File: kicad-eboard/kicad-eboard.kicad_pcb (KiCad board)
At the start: 2 copper layers, 92 parts, among them J1 Conn_01x02, J19 Conn_01x10, SW10 AMT10_Encoder, SW4 LIMIT_1, SW5 LIMIT_2, SW6 AMT10_Encoder, SW7 AMT10_Encoder, SW8 AMT10_Encoder, SW9 AMT10_Encoder, U1 TinkerBoard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

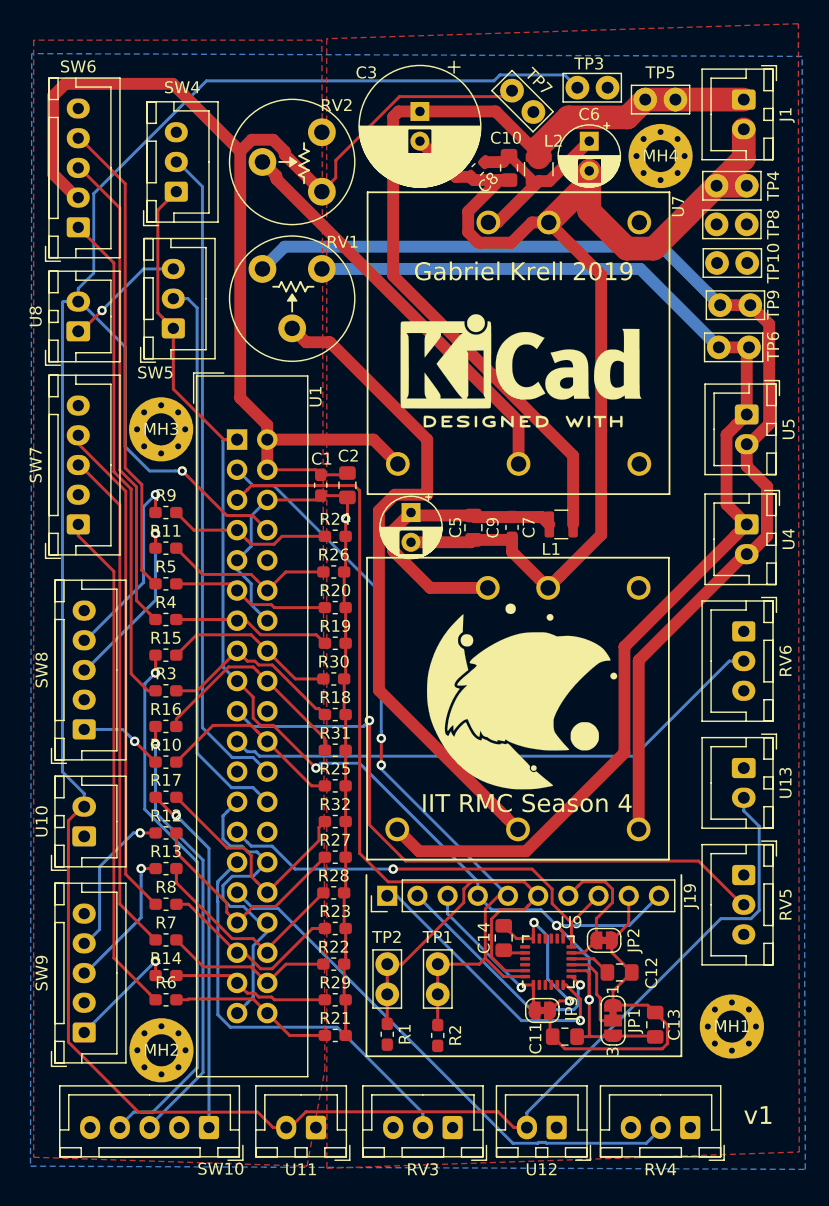
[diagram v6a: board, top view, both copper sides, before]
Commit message: Add readable test point silkscreens
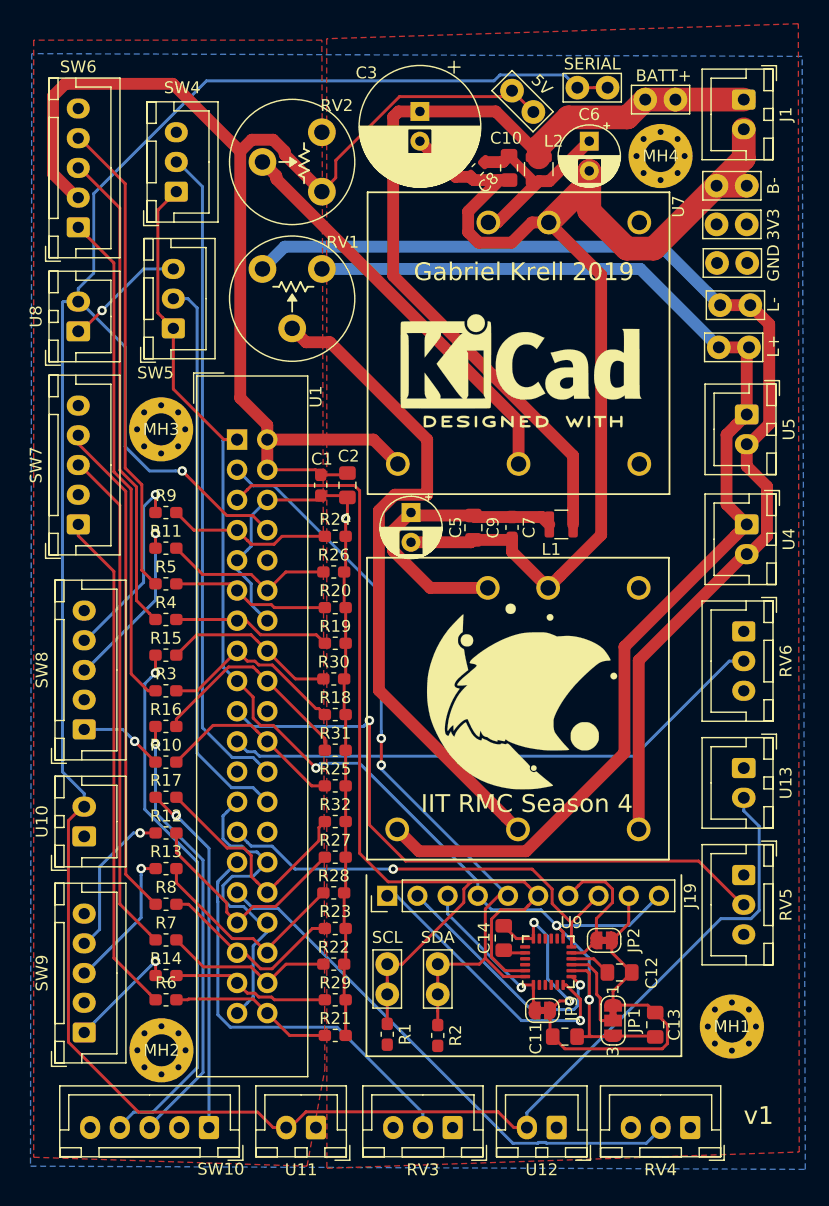
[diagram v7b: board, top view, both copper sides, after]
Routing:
- net Net-(TP3-Pad1): track 229.2 -> 231.7 mm
- net +5V: track 104.5 -> 107.0 mm
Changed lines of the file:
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@@
     (thickness 1.6)
     (drawings 6)
-    (tracks 673)
+    (tracks 676)
     (zones 0)
     (modules 92)
@@
     (descr "wire loop as test point, pitch 2.54mm, hole diameter 1.0mm, wire diameter 0.8mm")
     (tags "test point wire loop")
-    (fp_text reference TP8 (at -2.25 0 90) (layer F.SilkS)
+    (fp_text reference TP8 (at -2.25 0 90) (layer F.SilkS) hide
       (effects (font (size 1 1) (thickness 0.15)))
     )
@@
       (effects (font (size 1 1) (thickness 0.15)))
     )
-    (fp_text user %R (at 1.1 2.1) (layer F.Fab)
+    (fp_text user 3V3 (at -2.25 0 270) (layer F.SilkS)
       (effects (font (size 1 1) (thickness 0.15)))
     )
-    (fp_line (start -1.2 -1.2) (end -1.2 1.2) (layer F.SilkS) (width 0.12))
-    (fp_line (start -1.2 1.2) (end 3.7 1.2) (layer F.SilkS) (width 0.12))
-    (fp_line (start 3.7 1.2) (end 3.7 -1.2) (layer F.SilkS) (width 0.12))
-    (fp_line (start 3.7 -1.2) (end -1.2 -1.2) (layer F.SilkS) (width 0.12))
-    (fp_line (start 2.54 0) (end 0 0) (layer F.Fab) (width 0.12))
-    (fp_line (start -1.5 -1.5) (end 4.04 -1.5) (layer F.CrtYd) (width 0.05))
-    (fp_line (start -1.5 -1.5) (end -1.5 1.5) (layer F.CrtYd) (width 0.05))
-    (fp_line (start 4.04 1.5) (end 4.04 -1.5) (layer F.CrtYd) (width 0.05))
     (fp_line (start 4.04 1.5) (end -1.5 1.5) (layer F.CrtYd) (width 0.05))
-    (pad 1 thru_hole circle (at 0 0 180) (size 2 2) (drill 1) (layers *.Cu *.Mask)
-      (net 9 +3V3))
+    (fp_line (start 4.04 1.5) (end 4.04 -1.5) (layer F.CrtYd) (width 0.05))
+    (fp_line (start -1.5 -1.5) (end -1.5 1.5) (layer F.CrtYd) (width 0.05))
+    (fp_line (start -1.5 -1.5) (end 4.04 -1.5) (layer F.CrtYd) (width 0.05))
+    (fp_line (start 2.54 0) (end 0 0) (layer F.Fab) (width 0.12))
+    (fp_line (start 3.7 -1.2) (end -1.2 -1.2) (layer F.SilkS) (width 0.12))
+    (fp_line (start 3.7 1.2) (end 3.7 -1.2) (layer F.SilkS) (width 0.12))
+    (fp_line (start -1.2 1.2) (end 3.7 1.2) (layer F.SilkS) (width 0.12))
+    (fp_line (start -1.2 -1.2) (end -1.2 1.2) (layer F.SilkS) (width 0.12))
+    (fp_text user %R (at 1.1 2.1) (layer F.Fab)
+      (effects (font (size 1 1) (thickness 0.15)))
+    )
     (pad 1 thru_hole circle (at 2.54 0 180) (size 2 2) (drill 1) (layers *.Cu *.Mask)
       (net 9 +3V3))
+    (pad 1 thru_hole circle (at 0 0 180) (size 2 2) (drill 1) (layers *.Cu *.Mask)
+      (net 9 +3V3))
     (model ${KISYS3DMOD}/TestPoint.3dshapes/TestPoint_Bridge_Pitch2.54mm_Drill1.0mm.wrl
       (at (xyz 0 0 0))
@@
     (descr "wire loop as test point, pitch 2.54mm, hole diameter 1.0mm, wire diameter 0.8mm")
     (tags "test point wire loop")
-    (fp_text reference TP7 (at 1.06066 -2.12132 315) (layer F.SilkS)
+    (fp_text reference TP7 (at 1.06066 -2.12132 315) (layer F.SilkS) hide
       (effects (font (size 1 1) (thickness 0.15)))
     )
@@
       (effects (font (size 1 1) (thickness 0.15)))
     )
+    (fp_text user 5V (at 1.414214 -2.12132 315) (layer F.SilkS)
+      (effects (font (size 1 1) (thickness 0.15)))
+    )
     (pad 1 thru_hole circle (at 2.54 0 315) (size 2 2) (drill 1) (layers *.Cu *.Mask)
       (net 10 +5V))
@@
     (descr "wire loop as test point, pitch 2.54mm, hole diameter 1.0mm, wire diameter 0.8mm")
     (tags "test point wire loop")
-    (fp_text reference TP10 (at -2.21 0 90) (layer F.SilkS)
+    (fp_text reference TP10 (at -2.21 0 90) (layer F.SilkS) hide
       (effects (font (size 1 1) (thickness 0.15)))
     )
@@
       (effects (font (size 1 1) (thickness 0.15)))
     )
+    (fp_text user GND (at -2.21 0 270) (layer F.SilkS)
+      (effects (font (size 1 1) (thickness 0.15)))
+    )
     (pad 1 thru_hole circle (at 2.54 0 180) (size 2 2) (drill 1) (layers *.Cu *.Mask)
       (net 7 GND))
@@
     (descr "wire loop as test point, pitch 2.54mm, hole diameter 1.0mm, wire diameter 0.8mm")
     (tags "test point wire loop")
-    (fp_text reference TP3 (at 1 -2 180) (layer F.SilkS)
+    (fp_text reference TP3 (at 1 -2 180) (layer F.SilkS) hide
       (effects (font (size 1 1) (thickness 0.15)))
     )
@@
     (fp_line (start 4.04 1.5) (end 4.04 -1.5) (layer F.CrtYd) (width 0.05))
     (fp_line (start 4.04 1.5) (end -1.5 1.5) (layer F.CrtYd) (width 0.05))
+    (fp_text user SERIAL (at 1.25 -2) (layer F.SilkS)
+      (effects (font (size 1 1) (thickness 0.15)))
+    )
     (pad 1 thru_hole circle (at 0 0) (size 2 2) (drill 1) (layers *.Cu *.Mask)
       (net 3 "Net-(TP3-Pad1)"))
@@
     (descr "wire loop as test point, pitch 2.54mm, hole diameter 1.0mm, wire diameter 0.8mm")
     (tags "test point wire loop")
-    (fp_text reference TP9 (at -1.95 0.05 270) (layer F.SilkS)
+    (fp_text reference TP9 (at -1.95 0.05 270) (layer F.SilkS) hide
       (effects (font (size 1 1) (thickness 0.15)))
     )
@@
     (fp_line (start 4.04 1.5) (end 4.04 -1.5) (layer F.CrtYd) (width 0.05))
     (fp_line (start 4.04 1.5) (end -1.5 1.5) (layer F.CrtYd) (width 0.05))
+    (fp_text user L- (at -1.95 0.05 270) (layer F.SilkS)
+      (effects (font (size 1 1) (thickness 0.15)))
+    )
     (pad 1 thru_hole circle (at 0 0 180) (size 2 2) (drill 1) (layers *.Cu *.Mask)
       (net 8 GNDA))
@@
     (descr "wire loop as test point, pitch 2.54mm, hole diameter 1.0mm, wire diameter 0.8mm")
     (tags "test point wire loop")
-    (fp_text reference TP5 (at 1.25 2.25) (layer F.SilkS)
+    (fp_text reference TP5 (at 1.25 2.25) (layer F.SilkS) hide
       (effects (font (size 1 1) (thickness 0.15)))
     )
@@
     (fp_line (start 4.04 1.5) (end 4.04 -1.5) (layer F.CrtYd) (width 0.05))
     (fp_line (start 4.04 1.5) (end -1.5 1.5) (layer F.CrtYd) (width 0.05))
+    (fp_text user BATT+ (at 1 2 180) (layer F.SilkS)
+      (effects (font (size 1 1) (thickness 0.15)))
+    )
     (pad 1 thru_hole circle (at 0 0 180) (size 2 2) (drill 1) (layers *.Cu *.Mask)
       (net 6 +BATT))
@@
     (descr "wire loop as test point, pitch 2.54mm, hole diameter 1.0mm, wire diameter 0.8mm")
     (tags "test point wire loop")
-    (fp_text reference TP1 (at -2.25 0 180) (layer F.SilkS)
+    (fp_text reference TP1 (at -2.25 0 180) (layer F.SilkS) hide
       (effects (font (size 1 1) (thickness 0.15)))
     )
@@
       (effects (font (size 1 1) (thickness 0.15)))
     )
+    (fp_text user SDA (at -2.25 0) (layer F.SilkS)
+      (effects (font (size 1 1) (thickness 0.15)))
+    )
     (pad 1 thru_hole circle (at 2.54 0 270) (size 2 2) (drill 1) (layers *.Cu *.Mask)
       (net 5 /IMU/SDA))
@@
     (descr "wire loop as test point, pitch 2.54mm, hole diameter 1.0mm, wire diameter 0.8mm")
     (tags "test point wire loop")
-    (fp_text reference TP2 (at -2.25 0 180) (layer F.SilkS)
+    (fp_text reference TP2 (at -2.25 0 180) (layer F.SilkS) hide
       (effects (font (size 1 1) (thickness 0.15)))
     )
@@
     (fp_line (start 4.04 1.5) (end 4.04 -1.5) (layer F.CrtYd) (width 0.05))
     (fp_line (start 4.04 1.5) (end -1.5 1.5) (layer F.CrtYd) (width 0.05))
+    (fp_text user SCL (at -2.25 0) (layer F.SilkS)
+      (effects (font (size 1 1) (thickness 0.15)))
+    )
     (pad 1 thru_hole circle (at 0 0 270) (size 2 2) (drill 1) (layers *.Cu *.Mask)
       (net 4 /IMU/SCL))
@@
     (descr "wire loop as test point, pitch 2.54mm, hole diameter 1.0mm, wire diameter 0.8mm")
     (tags "test point wire loop")
-    (fp_text reference TP4 (at -2.25 0 90) (layer F.SilkS)
+    (fp_text reference TP4 (at -2.25 0 90) (layer F.SilkS) hide
       (effects (font (size 1 1) (thickness 0.15)))
     )
@@
     (fp_line (start 4.04 1.5) (end 4.04 -1.5) (layer F.CrtYd) (width 0.05))
     (fp_line (start 4.04 1.5) (end -1.5 1.5) (layer F.CrtYd) (width 0.05))
+    (fp_text user B- (at -2.25 0 270) (layer F.SilkS)
+      (effects (font (size 1 1) (thickness 0.15)))
+    )
     (pad 1 thru_hole circle (at 0 0 180) (size 2 2) (drill 1) (layers *.Cu *.Mask)
       (net 2 GNDPWR))
@@
     (descr "wire loop as test point, pitch 2.54mm, hole diameter 1.0mm, wire diameter 0.8mm")
     (tags "test point wire loop")
-    (fp_text reference TP6 (at 4.6 -0.1 270) (layer F.SilkS)
+    (fp_text reference TP6 (at 4.6 -0.1 270) (layer F.SilkS) hide
       (effects (font (size 1 1) (thickness 0.15)))
     )
@@
       (effects (font (size 1 1) (thickness 0.15)))
     )
+    (fp_text user L+ (at 4.6 -0.1 90) (layer F.SilkS)
+      (effects (font (size 1 1) (thickness 0.15)))
+    )
     (pad 1 thru_hole circle (at 2.54 0) (size 2 2) (drill 1) (layers *.Cu *.Mask)
       (net 1 +12V))
@@
   (segment (start 52.485999 15.174999) (end 52.985999 14.674999) (width 0.25) (layer B.Cu) (net 3))
   (segment (start 28.288286 15.174999) (end 52.485999 15.174999) (width 0.25) (layer B.Cu) (net 3))
+  (segment (start 60.914213 15.75) (end 62.04 15.75) (width 0.25) (layer F.Cu) (net 3))
+  (segment (start 59.5 15.75) (end 60.914213 15.75) (width 0.25) (layer F.Cu) (net 3))
   (segment (start 43.5 90.914213) (end 43.5 92.04) (width 0.25) (layer F.Cu) (net 4))
   (segment (start 43.5 89.5) (end 43.5 90.914213) (width 0.25) (layer F.Cu) (net 4))
@@
   (segment (start 16.408269 15.424991) (end 15.374979 16.458281) (width 1) (layer F.Cu) (net 10))
   (segment (start 25.452591 15.424991) (end 16.408269 15.424991) (width 1) (layer F.Cu) (net 10))
+  (segment (start 54 16) (end 55.796051 17.796051) (width 0.25) (layer F.Cu) (net 10))
   (segment (start 55.8 93.3) (end 55.9 93.4) (width 0.25) (layer F.Cu) (net 11))
   (segment (start 55.8 91.25) (end 55.8 93.3) (width 0.25) (layer F.Cu) (net 11))

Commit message: Clean up perimeter silkscreen
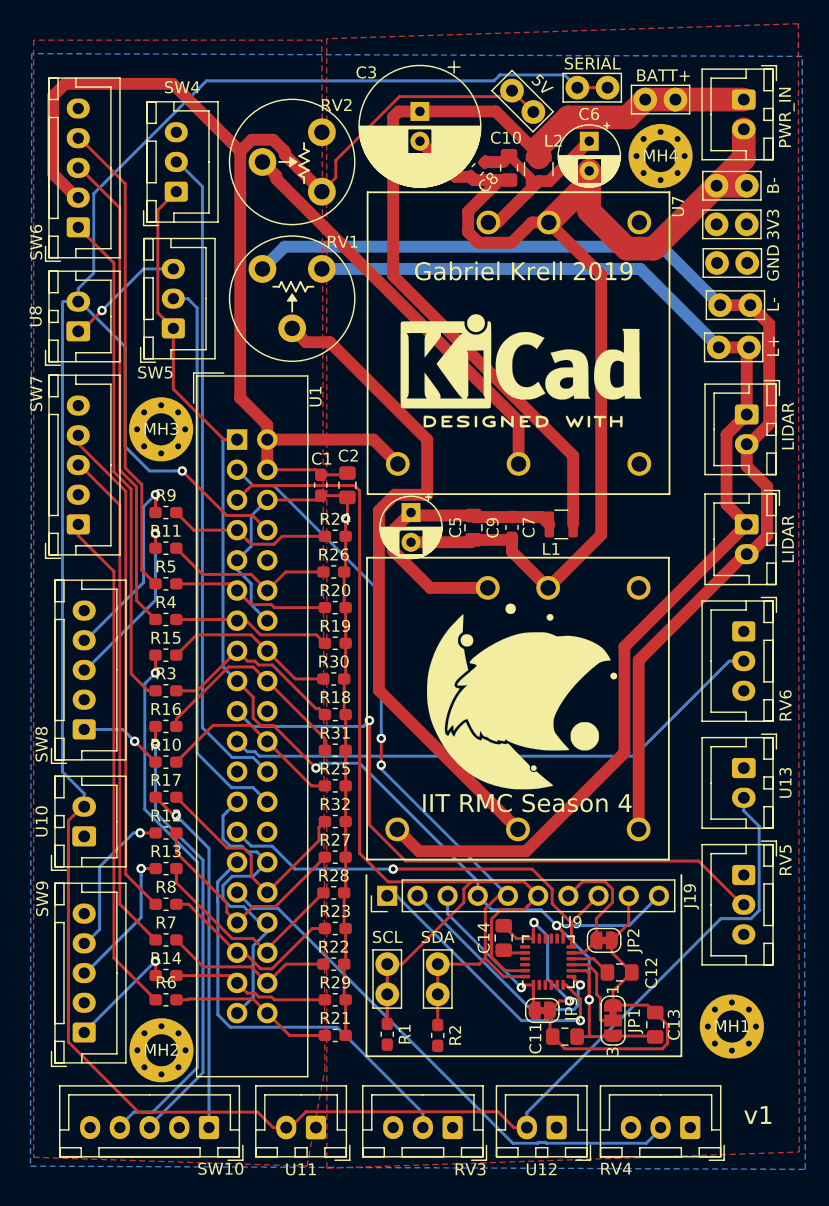
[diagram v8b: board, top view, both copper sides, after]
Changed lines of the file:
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@@
     (descr "JST XH series connector, B3B-XH-A (http://www.jst-mfg.com/product/pdf/eng/eXH.pdf), generated with kicad-footprint-generator")
     (tags "connector JST XH vertical")
-    (fp_text reference RV5 (at 2.5 -3.55 90) (layer F.SilkS)
+    (fp_text reference RV5 (at -1.25 -3.55 90) (layer F.SilkS)
       (effects (font (size 1 1) (thickness 0.15)))
     )
@@
     (descr "JST XH series connector, B3B-XH-A (http://www.jst-mfg.com/product/pdf/eng/eXH.pdf), generated with kicad-footprint-generator")
     (tags "connector JST XH vertical")
-    (fp_text reference RV6 (at 2.5 -3.55 90) (layer F.SilkS)
+    (fp_text reference RV6 (at 6.25 -3.55 90) (layer F.SilkS)
       (effects (font (size 1 1) (thickness 0.15)))
     )
@@
     (descr "JST XH series connector, B3B-XH-A (http://www.jst-mfg.com/product/pdf/eng/eXH.pdf), generated with kicad-footprint-generator")
     (tags "connector JST XH vertical")
-    (fp_text reference RV3 (at 2.5 -3.55) (layer F.SilkS)
+    (fp_text reference RV3 (at -1.5 -3.55) (layer F.SilkS)
       (effects (font (size 1 1) (thickness 0.15)))
     )
@@
     (descr "JST XH series connector, B2B-XH-A (http://www.jst-mfg.com/product/pdf/eng/eXH.pdf), generated with kicad-footprint-generator")
     (tags "connector JST XH vertical")
-    (fp_text reference J1 (at 1.25 -3.55 90) (layer F.SilkS)
+    (fp_text reference J1 (at 1.25 -3.55 90) (layer F.SilkS) hide
       (effects (font (size 1 1) (thickness 0.15)))
     )
@@
     (fp_line (start -2.85 -2.75) (end -2.85 -1.5) (layer F.SilkS) (width 0.12))
     (fp_text user %R (at 1.25 2.7 90) (layer F.Fab)
+      (effects (font (size 1 1) (thickness 0.15)))
+    )
+    (fp_text user PWR_IN (at 1.5 -3.5 270) (layer F.SilkS)
       (effects (font (size 1 1) (thickness 0.15)))
     )
@@
     (descr "JST XH series connector, B2B-XH-A (http://www.jst-mfg.com/product/pdf/eng/eXH.pdf), generated with kicad-footprint-generator")
     (tags "connector JST XH vertical")
-    (fp_text reference U4 (at 1.25 -3.55 90) (layer F.SilkS)
+    (fp_text reference U4 (at 1.25 -3.55 90) (layer F.SilkS) hide
       (effects (font (size 1 1) (thickness 0.15)))
     )
@@
     (fp_line (start -2.45 3.4) (end 4.95 3.4) (layer F.Fab) (width 0.1))
     (fp_line (start -2.45 -2.35) (end -2.45 3.4) (layer F.Fab) (width 0.1))
+    (fp_text user LIDAR (at 1.25 -3.5 270) (layer F.SilkS)
+      (effects (font (size 1 1) (thickness 0.15)))
+    )
     (pad 2 thru_hole oval (at 2.5 0 270) (size 1.7 2) (drill 1) (layers *.Cu *.Mask)
       (net 8 GNDA))
@@
     (descr "JST XH series connector, B2B-XH-A (http://www.jst-mfg.com/product/pdf/eng/eXH.pdf), generated with kicad-footprint-generator")
     (tags "connector JST XH vertical")
-    (fp_text reference U5 (at 1.25 -3.55 90) (layer F.SilkS)
+    (fp_text reference U5 (at 1.25 -3.55 90) (layer F.SilkS) hide
       (effects (font (size 1 1) (thickness 0.15)))
     )
@@
     (fp_line (start -2.45 3.4) (end 4.95 3.4) (layer F.Fab) (width 0.1))
     (fp_line (start -2.45 -2.35) (end -2.45 3.4) (layer F.Fab) (width 0.1))
+    (fp_text user LIDAR (at 1 -3.5 270) (layer F.SilkS)
+      (effects (font (size 1 1) (thickness 0.15)))
+    )
     (pad 2 thru_hole oval (at 2.5 0 270) (size 1.7 2) (drill 1) (layers *.Cu *.Mask)
       (net 8 GNDA))
@@
     (descr "JST XH series connector, B3B-XH-A (http://www.jst-mfg.com/product/pdf/eng/eXH.pdf), generated with kicad-footprint-generator")
     (tags "connector JST XH vertical")
-    (fp_text reference RV4 (at 2.5 -3.55) (layer F.SilkS)
+    (fp_text reference RV4 (at 6.25 -3.5) (layer F.SilkS)
       (effects (font (size 1 1) (thickness 0.15)))
     )
@@
     (descr "JST XH series connector, B5B-XH-A (http://www.jst-mfg.com/product/pdf/eng/eXH.pdf), generated with kicad-footprint-generator")
     (tags "connector JST XH vertical")
-    (fp_text reference SW6 (at 13.5 0) (layer F.SilkS)
+    (fp_text reference SW6 (at -1.25 -3.5 90) (layer F.SilkS)
       (effects (font (size 1 1) (thickness 0.15)))
     )
@@
     (descr "JST XH series connector, B5B-XH-A (http://www.jst-mfg.com/product/pdf/eng/eXH.pdf), generated with kicad-footprint-generator")
     (tags "connector JST XH vertical")
-    (fp_text reference SW7 (at 5 -3.55 270) (layer F.SilkS)
+    (fp_text reference SW7 (at 11 -3.5 270) (layer F.SilkS)
       (effects (font (size 1 1) (thickness 0.15)))
     )
@@
     (descr "JST XH series connector, B5B-XH-A (http://www.jst-mfg.com/product/pdf/eng/eXH.pdf), generated with kicad-footprint-generator")
     (tags "connector JST XH vertical")
-    (fp_text reference SW8 (at 5 -3.55 270) (layer F.SilkS)
+    (fp_text reference SW8 (at -1.25 -3.55 270) (layer F.SilkS)
       (effects (font (size 1 1) (thickness 0.15)))
     )
@@
     (descr "JST XH series connector, B5B-XH-A (http://www.jst-mfg.com/product/pdf/eng/eXH.pdf), generated with kicad-footprint-generator")
     (tags "connector JST XH vertical")
-    (fp_text reference SW9 (at 5 -3.55 270) (layer F.SilkS)
-      (effects (font (size 1 1) (thickness 0.15)))
-    )
+    (fp_text reference SW9 (at 11.25 -3.5 270) (layer F.SilkS)
+      (effects (font (size 1 1) (thickness 0.15)))
+    )
